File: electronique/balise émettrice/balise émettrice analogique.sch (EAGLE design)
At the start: 47 parts, among them IC1 TL084P, IC2 TL084P

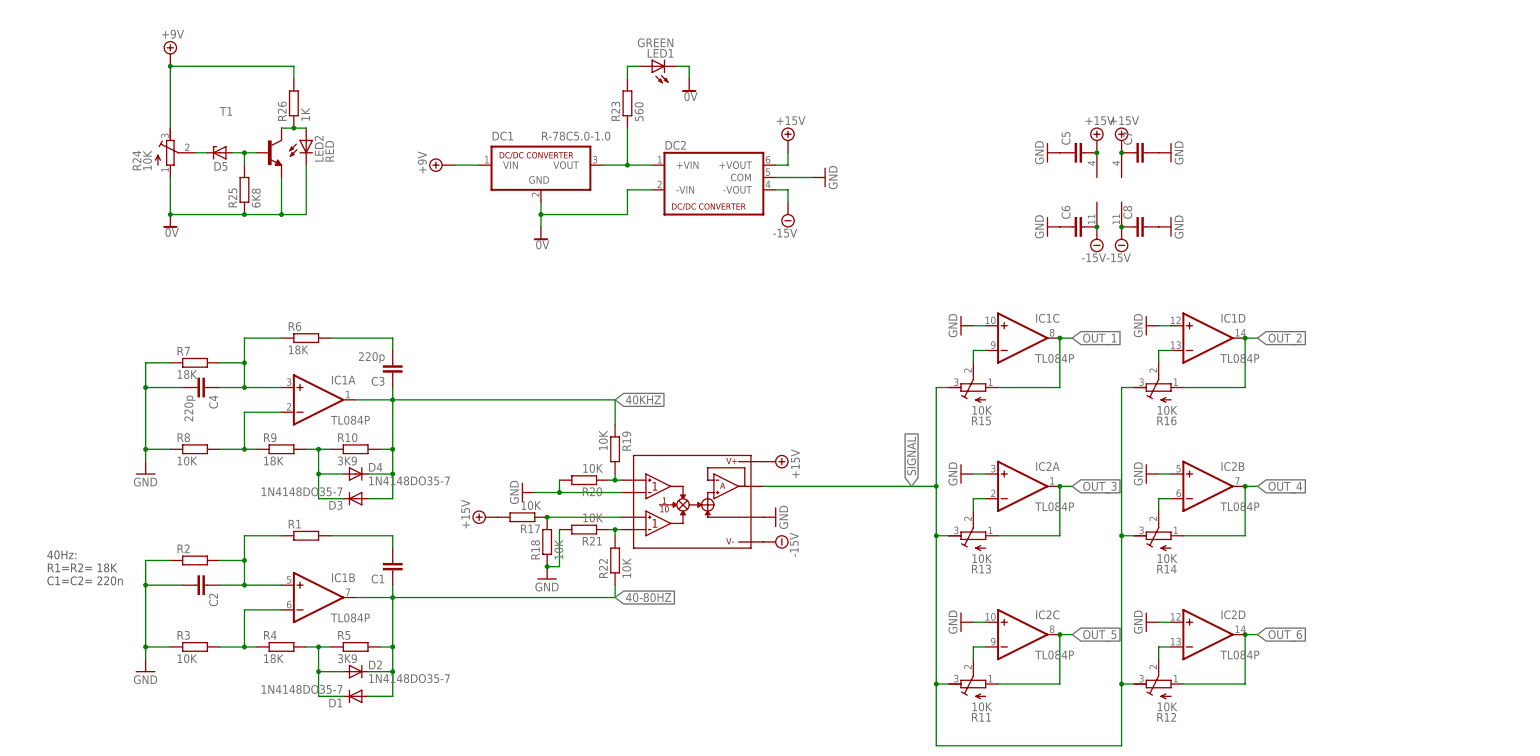
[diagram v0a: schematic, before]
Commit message: maj elec balise emettrice
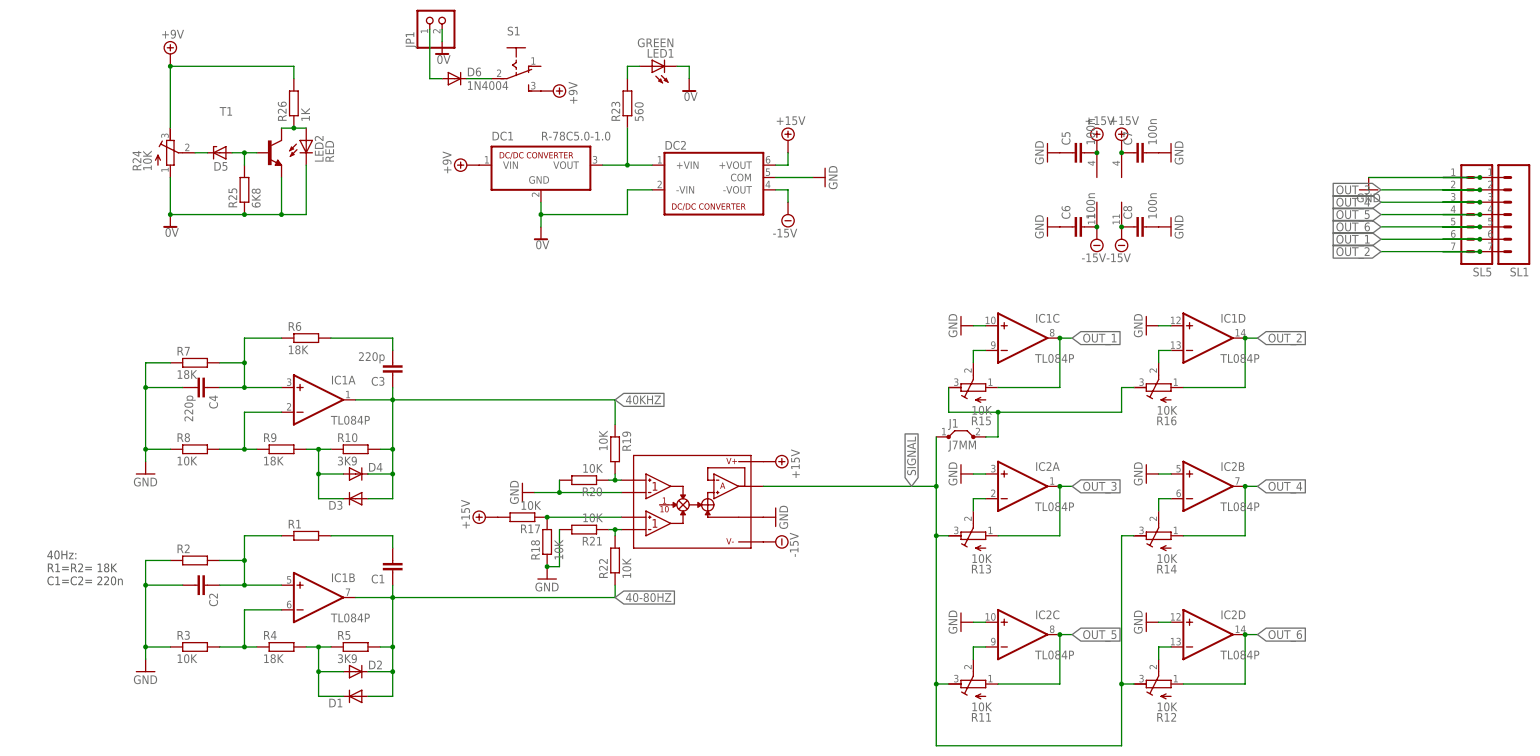
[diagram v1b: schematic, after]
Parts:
- added D6: 1N4004, diode:1N4004
- added J1: J7MM, jumper:J7MM
- added JP1: (no value), pinhead:PINHD-1X2
- added S1: (no value), switch:255SB
- added SL1, SL5: (no value), con-amp-quick:M07
- C5, C6, C7, C8: value (none) -> 100n
- D1, D2, D3, D4: value 1N4148DO35-7 -> (none); device diode:1N4148DO35-7 -> diode:DIODE-D-2.5
- R1, R10, R17, R18, R19, R20, R21, R22, R25, R26, R3, R4, R5, R6, R7, R8, R9: device resistor:R-EU_0204/7 -> resistor:R-EU_0207/2V
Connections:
- new net N$20: D6.A, JP1.1
- new net N$23: D6.C, S1.P
- new net N$25: J1.2, R15.A, R16.A
- net +9V: now also S1.S
- net 0V: now also JP1.2
- net GND: now also SL1.1, SL5.1
- net OUT_1: now also SL1.6, SL5.6
- net OUT_2: now also SL1.7, SL5.7
- net OUT_3: now also SL1.2, SL5.2
- net OUT_4: now also SL1.3, SL5.3
- net OUT_5: now also SL1.4, SL5.4
- net OUT_6: now also SL1.5, SL5.5
- net SIGNAL: now also J1.1; no longer R15.A, R16.A

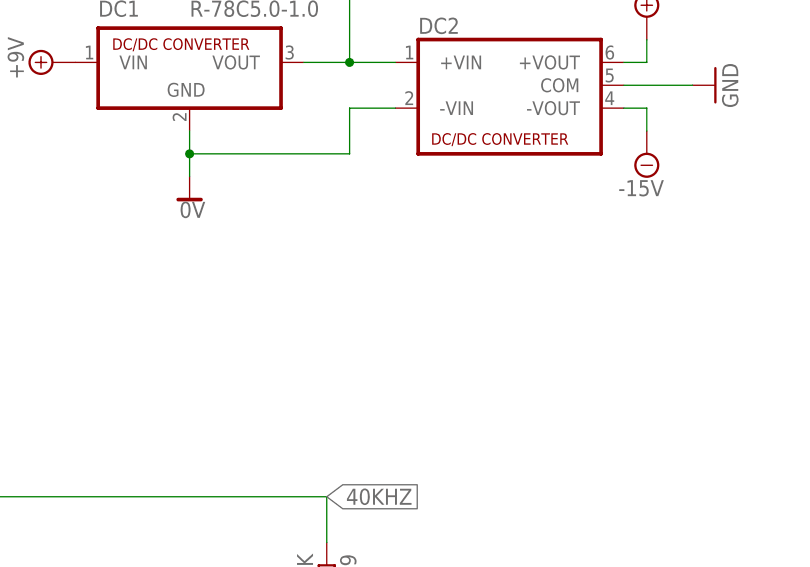
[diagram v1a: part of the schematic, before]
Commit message: correctif equations des filtres + ajout debut circuit de reception
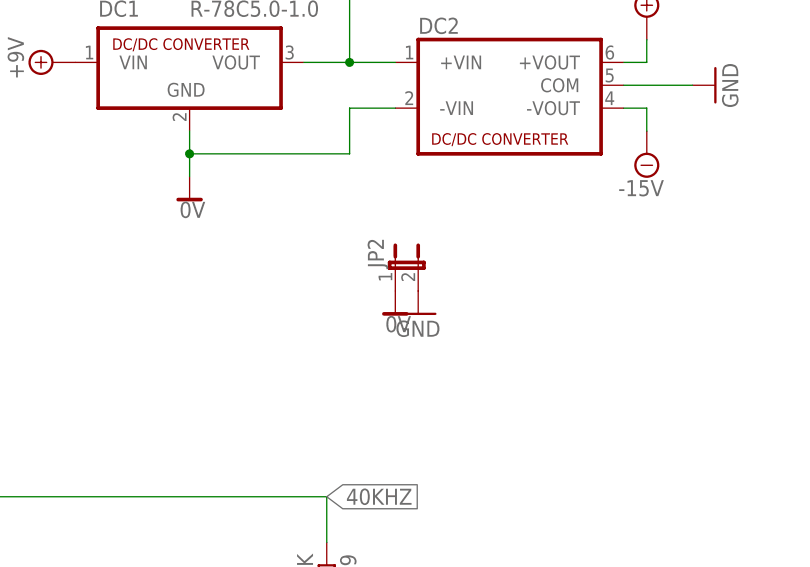
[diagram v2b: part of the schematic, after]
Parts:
- added JP2: (no value), jumper:JP1E
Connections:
- net 0V: now also JP2.1
- net GND: now also JP2.2
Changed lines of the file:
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@@
 <attribute name="OC_NEWARK" value="unknown"/>
 </part>
+<part name="JP2" library="jumper" deviceset="JP1E" device=""/>
+<part name="SUPPLY17" library="supply2" deviceset="0V" device=""/>
+<part name="GND18" library="supply1" deviceset="GND" device=""/>
 </parts>
 <sheets>
@@
 <instance part="SL5" gate="G$1" x="289.56" y="91.44" rot="R180"/>
 <instance part="SL1" gate="G$1" x="297.18" y="91.44" rot="R180"/>
+<instance part="JP2" gate="A" x="121.92" y="76.2"/>
+<instance part="SUPPLY17" gate="0V" x="121.92" y="71.12"/>
+<instance part="GND18" gate="1" x="124.46" y="71.12"/>
 </instances>
 <busses>
@@
 <junction x="292.1" y="96.52"/>
 <wire x1="292.1" y1="96.52" x2="284.48" y2="96.52" width="0.1524" layer="91"/>
+</segment>
+<segment>
+<pinref part="JP2" gate="A" pin="2"/>
+<pinref part="GND18" gate="1" pin="GND"/>
 </segment>
 </net>
@@
 <wire x1="78.74" y1="124.46" x2="78.74" y2="127" width="0.1524" layer="91"/>
 </segment>
-</net>
+<segment>
+<pinref part="JP2" gate="A" pin="1"/>
+<pinref part="SUPPLY17" gate="0V" pin="0V"/>
+</segment>
+</net>

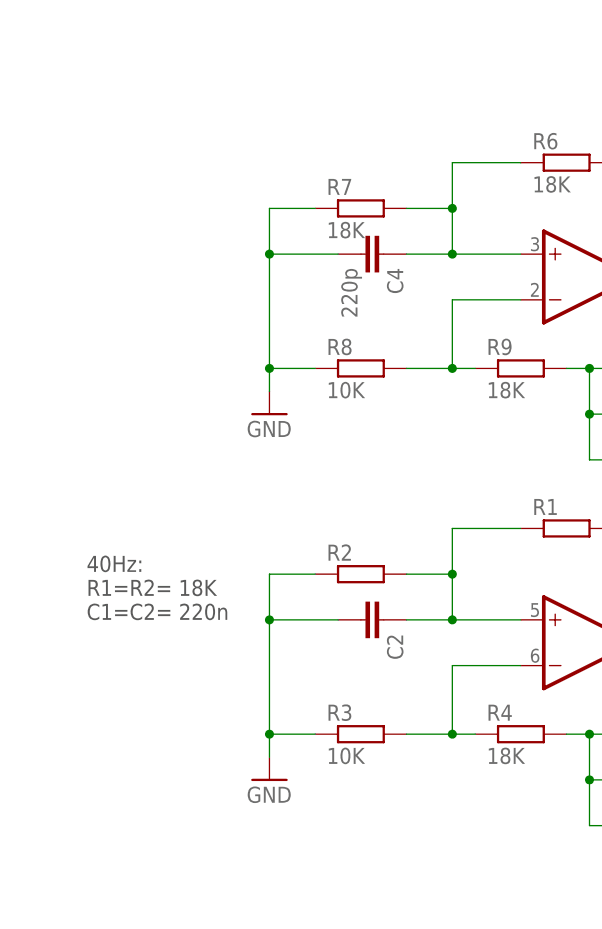
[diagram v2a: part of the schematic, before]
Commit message: maj filtrage + ajout routage balise receptrice, partie filtrage
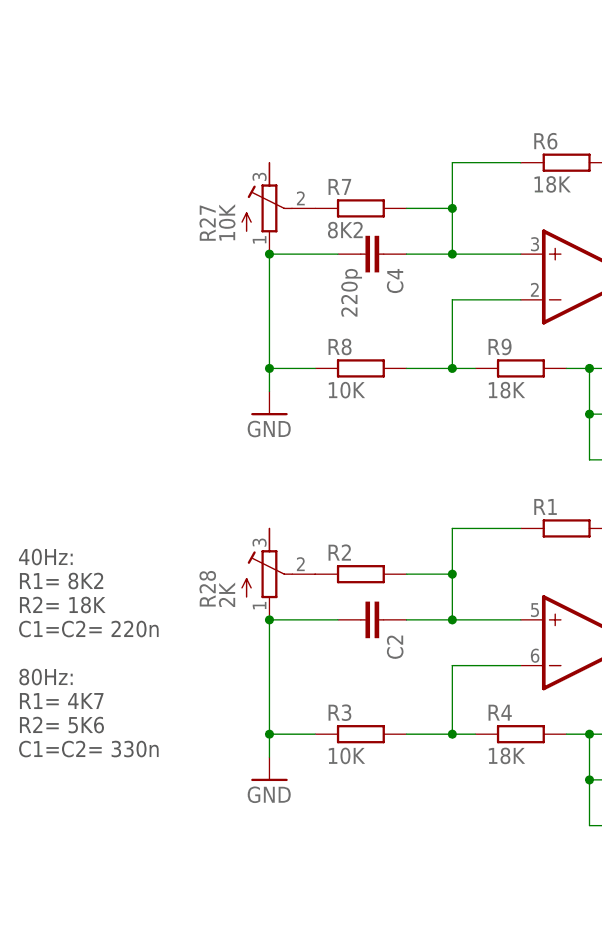
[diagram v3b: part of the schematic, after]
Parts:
- added R27: 10K, resistor:R-TRIMM3339P
- added R28: 2K, resistor:R-TRIMM3339P
- R7: value 18K -> 8K2
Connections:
- new net N$26: R27.S, R7.1
- new net N$27: R2.1, R28.S
- net GND: now also R27.E, R28.E; no longer R2.1, R7.1
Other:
- note added: "40Hz: R1= 8K2 R2= 18K C1=C2= 220n 80Hz: R1= 4K7 R2= 5K6 C1=C2= 330n"
- note removed: "40Hz: R1=R2= 18K C1=C2= 220n"
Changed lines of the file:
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@@
 <part name="C3" library="resistor" deviceset="C-EU" device="075-032X103" value="220p"/>
 <part name="GND3" library="supply1" deviceset="GND" device=""/>
-<part name="R7" library="resistor" deviceset="R-EU_" device="0207/2V" value="18K"/>
+<part name="R7" library="resistor" deviceset="R-EU_" device="0207/2V" value="8K2"/>
 <part name="R8" library="resistor" deviceset="R-EU_" device="0207/2V" value="10K"/>
 <part name="R9" library="resistor" deviceset="R-EU_" device="0207/2V" value="18K"/>
@@
 <part name="SUPPLY17" library="supply2" deviceset="0V" device=""/>
 <part name="GND18" library="supply1" deviceset="GND" device=""/>
+<part name="R27" library="resistor" deviceset="R-TRIMM" device="3339P" value="10K"/>
+<part name="R28" library="resistor" deviceset="R-TRIMM" device="3339P" value="2K"/>
 </parts>
 <sheets>
 <sheet>
 <plain>
-<text x="-2.54" y="12.7" size="1.778" layer="97">40Hz:
-R1=R2= 18K
-C1=C2= 220n</text>
+<text x="-10.16" y="-2.54" size="1.778" layer="97">40Hz:
+R1= 8K2
+R2= 18K
+C1=C2= 220n
+80Hz:
+R1= 4K7
+R2= 5K6
+C1=C2= 330n</text>
 </plain>
 <instances>
@@
 <instance part="SUPPLY17" gate="0V" x="121.92" y="71.12"/>
 <instance part="GND18" gate="1" x="124.46" y="71.12"/>
+<instance part="R27" gate="G$1" x="17.78" y="58.42"/>
+<instance part="R28" gate="G$1" x="17.78" y="17.78"/>
 </instances>
 <busses>
@@
 <pinref part="GND3" gate="1" pin="GND"/>
 <wire x1="22.86" y1="40.64" x2="17.78" y2="40.64" width="0.1524" layer="91"/>
-<pinref part="R7" gate="G$1" pin="1"/>
 <wire x1="17.78" y1="40.64" x2="17.78" y2="38.1" width="0.1524" layer="91"/>
-<wire x1="22.86" y1="58.42" x2="17.78" y2="58.42" width="0.1524" layer="91"/>
-<wire x1="17.78" y1="58.42" x2="17.78" y2="53.34" width="0.1524" layer="91"/>
 <junction x="17.78" y="40.64"/>
 <pinref part="C4" gate="G$1" pin="2"/>
 <wire x1="17.78" y1="53.34" x2="17.78" y2="40.64" width="0.1524" layer="91"/>
 <wire x1="25.4" y1="53.34" x2="17.78" y2="53.34" width="0.1524" layer="91"/>
+<pinref part="R27" gate="G$1" pin="E"/>
 <junction x="17.78" y="53.34"/>
 </segment>
@@
 <pinref part="GND1" gate="1" pin="GND"/>
 <wire x1="22.86" y1="0" x2="17.78" y2="0" width="0.1524" layer="91"/>
-<pinref part="R2" gate="G$1" pin="1"/>
 <wire x1="17.78" y1="0" x2="17.78" y2="-2.54" width="0.1524" layer="91"/>
-<wire x1="22.86" y1="17.78" x2="17.78" y2="17.78" width="0.1524" layer="91"/>
-<wire x1="17.78" y1="17.78" x2="17.78" y2="12.7" width="0.1524" layer="91"/>
 <junction x="17.78" y="0"/>
 <pinref part="C2" gate="G$1" pin="2"/>
 <wire x1="17.78" y1="12.7" x2="17.78" y2="0" width="0.1524" layer="91"/>
 <wire x1="25.4" y1="12.7" x2="17.78" y2="12.7" width="0.1524" layer="91"/>
+<pinref part="R28" gate="G$1" pin="E"/>
 <junction x="17.78" y="12.7"/>
 </segment>
@@
 </segment>
 </net>
+<net name="N$26" class="0">
+<segment>
+<pinref part="R7" gate="G$1" pin="1"/>
+<pinref part="R27" gate="G$1" pin="S"/>
+</segment>
+</net>
+<net name="N$27" class="0">
+<segment>
+<pinref part="R2" gate="G$1" pin="1"/>
+<pinref part="R28" gate="G$1" pin="S"/>
+</segment>
+</net>

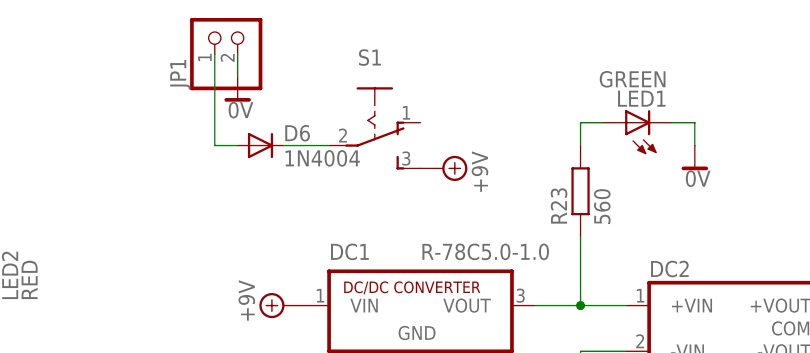
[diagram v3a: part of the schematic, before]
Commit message: maj balise emettrice : ajout de la DEL de debug + interrupteur dans le modele 3D
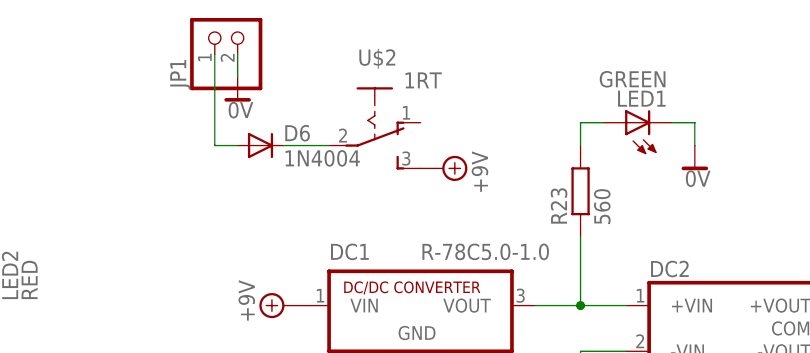
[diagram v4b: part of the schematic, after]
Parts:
- removed S1: (no value), switch:255SB
- added U$2: 1RT, switch:1RT
- C1, C2, C5, C6, C7, C8, D1, D2, D3, D4, D5, D6, DC1, IC1, IC2, J1, JP1, JP2, LED1, LED2, R1, R10, R11, R12, R13, R14, R15, R16, R17, R18, R19, R2, R20, R21, R22, R23, R24, R25, R26, R27, R28, R3, R4, R5, R6, R7, R8, R9, SL5, T1, U$1: OC_FARNELL (none) -> unknown
- C3, C4: MF (none) -> PANASONIC ELECTRONIC COMPONENTS; MPN (none) -> EEE1EA220SP; OC_FARNELL (none) -> 9696970
- DC2: MF (none) -> MURATA POWER SOLUTIONS; MPN (none) -> NMA1205DC; OC_FARNELL (none) -> 1021434
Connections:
- net +9V: now also U$2.S; no longer S1.S
- net N$23: now also U$2.P; no longer S1.P
